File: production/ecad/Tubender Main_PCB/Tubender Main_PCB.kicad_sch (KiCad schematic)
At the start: 0 parts

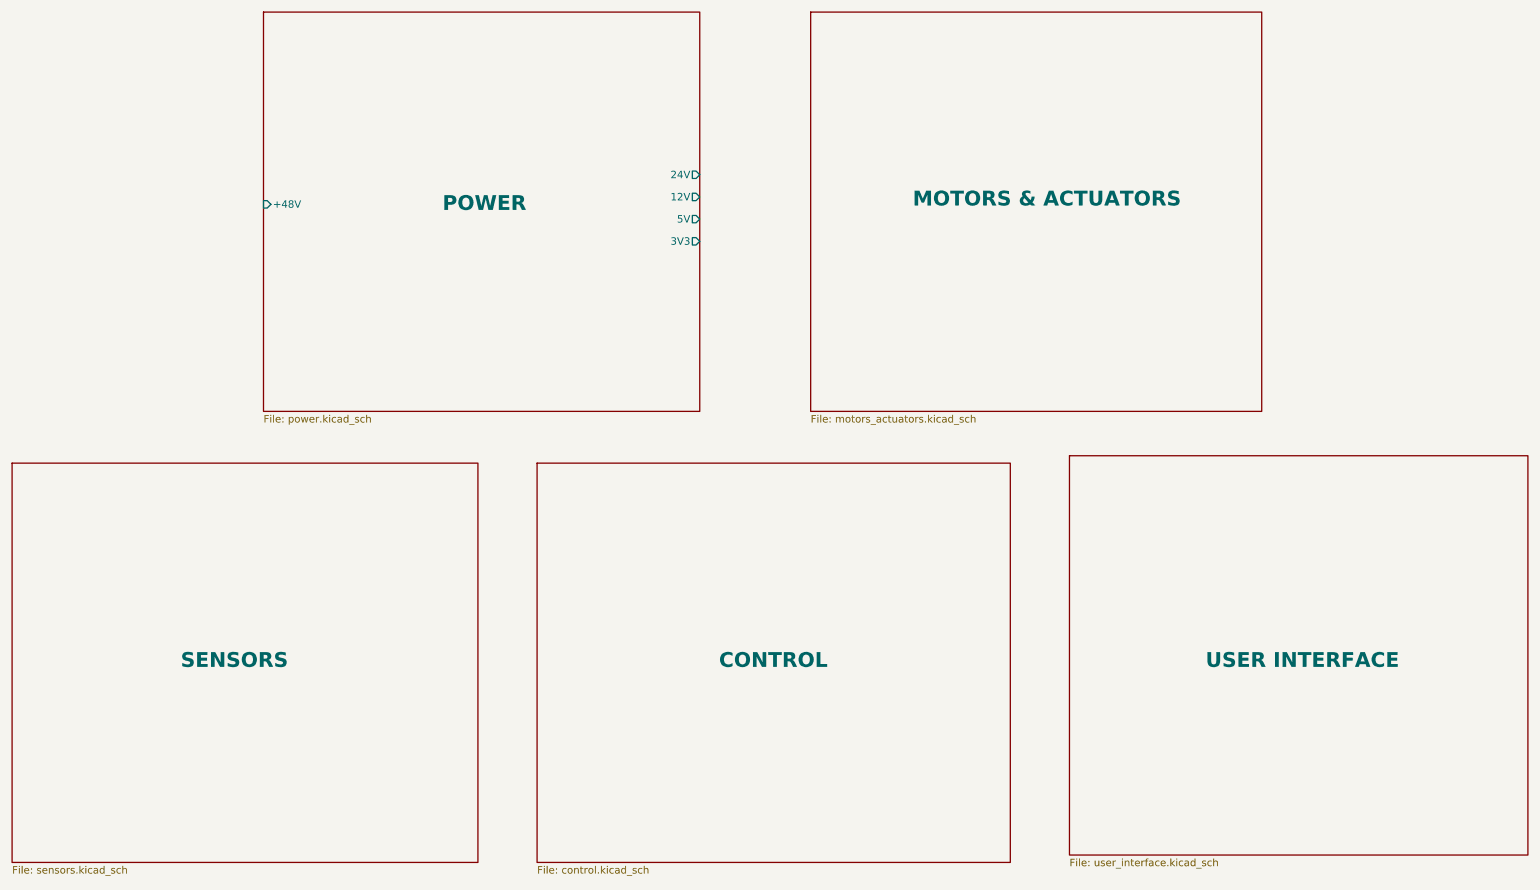
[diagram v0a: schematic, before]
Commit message: Separated into Two PCBS
UI and Main now seperated
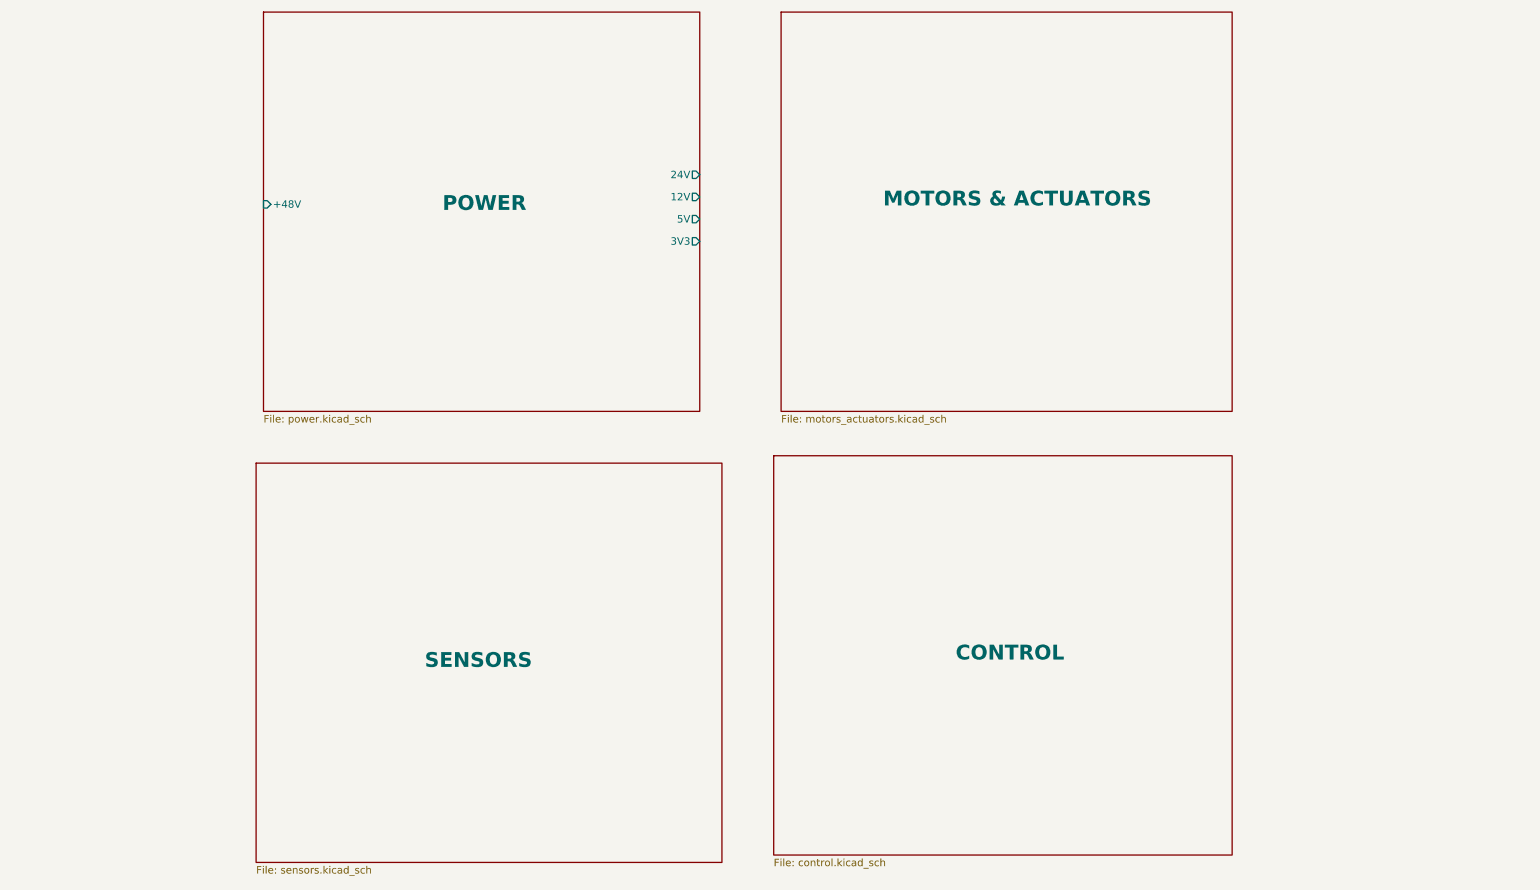
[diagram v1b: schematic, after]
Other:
- removed sheet USER INTERFACE
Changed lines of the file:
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@@
 	)
 	(sheet
-		(at 153.67 17.78)
+		(at 148.59 17.78)
 		(size 77.47 68.58)
 		(stroke
@@
 		)
 		(property "Sheetname" "MOTORS & ACTUATORS"
-			(at 171.196 51.308 0)
+			(at 166.116 51.308 0)
 			(effects
 				(font
@@
 		)
 		(property "Sheetfile" "motors_actuators.kicad_sch"
-			(at 153.67 86.9446 0)
+			(at 148.59 86.9446 0)
 			(effects
 				(font
@@
 		)
 		(instances
-			(project "Tubender PCB"
+			(project "Tubender Main_PCB"
 				(path "/3e1aedd0-6089-4edb-92c7-0c31da2e7927"
 					(page "3")
@@
 		)
 		(instances
-			(project "Tubender PCB"
+			(project "Tubender Main_PCB"
 				(path "/3e1aedd0-6089-4edb-92c7-0c31da2e7927"
 					(page "2")
@@
 	)
 	(sheet
-		(at 106.68 95.25)
-		(size 81.28 68.58)
+		(at 147.32 93.98)
+		(size 78.74 68.58)
 		(stroke
 			(width 0.1524)
@@
 		)
 		(property "Sheetname" "CONTROL"
-			(at 137.922 130.556 0)
+			(at 178.562 129.286 0)
 			(effects
 				(font
@@
 		)
 		(property "Sheetfile" "control.kicad_sch"
-			(at 106.68 164.4146 0)
+			(at 147.32 163.1446 0)
 			(effects
 				(font
@@
 		)
 		(instances
-			(project "Tubender PCB"
+			(project "Tubender Main_PCB"
 				(path "/3e1aedd0-6089-4edb-92c7-0c31da2e7927"
 					(page "5")
@@
 	)
 	(sheet
-		(at 16.51 95.25)
+		(at 58.42 95.25)
 		(size 80.01 68.58)
 		(stroke
@@
 		)
 		(property "Sheetname" "SENSORS"
-			(at 45.466 130.556 0)
+			(at 87.376 130.556 0)
 			(effects
 				(font
@@
 		)
 		(property "Sheetfile" "sensors.kicad_sch"
-			(at 16.51 164.4146 0)
+			(at 58.42 164.4146 0)
 			(effects
 				(font
@@
 		)
 		(instances
-			(project "Tubender PCB"
+			(project "Tubender Main_PCB"
 				(path "/3e1aedd0-6089-4edb-92c7-0c31da2e7927"
 					(page "4")
 				)
 			)
-		)
-	)
-	(sheet
-		(at 198.12 93.98)
-		(size 78.74 68.58)
-		(stroke
-			(width 0.1524)
-			(type solid)
-		)
-		(fill
-			(color 0 0 0 0.0000)
-		)
-		(property "Sheetname" "USER INTERFACE"
-			(at 221.488 130.556 0)
-			(effects
-				(font
-					(size 2.54 2.54)
-					(thickness 0.508)
-					(bold yes)
-				)
-				(justify left bottom)
-			)
-		)
-		(property "Sheetfile" "user_interface.kicad_sch"
-			(at 198.12 163.1446 0)
-			(effects
-				(font
-					(size 1.27 1.27)
-				)
-				(justify left top)
-			)
-		)
-		(instances
-			(project "Tubender PCB"
-				(path "/3e1aedd0-6089-4edb-92c7-0c31da2e7927"
-					(page "6")
-				)
-			)

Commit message: Fixed the Nets
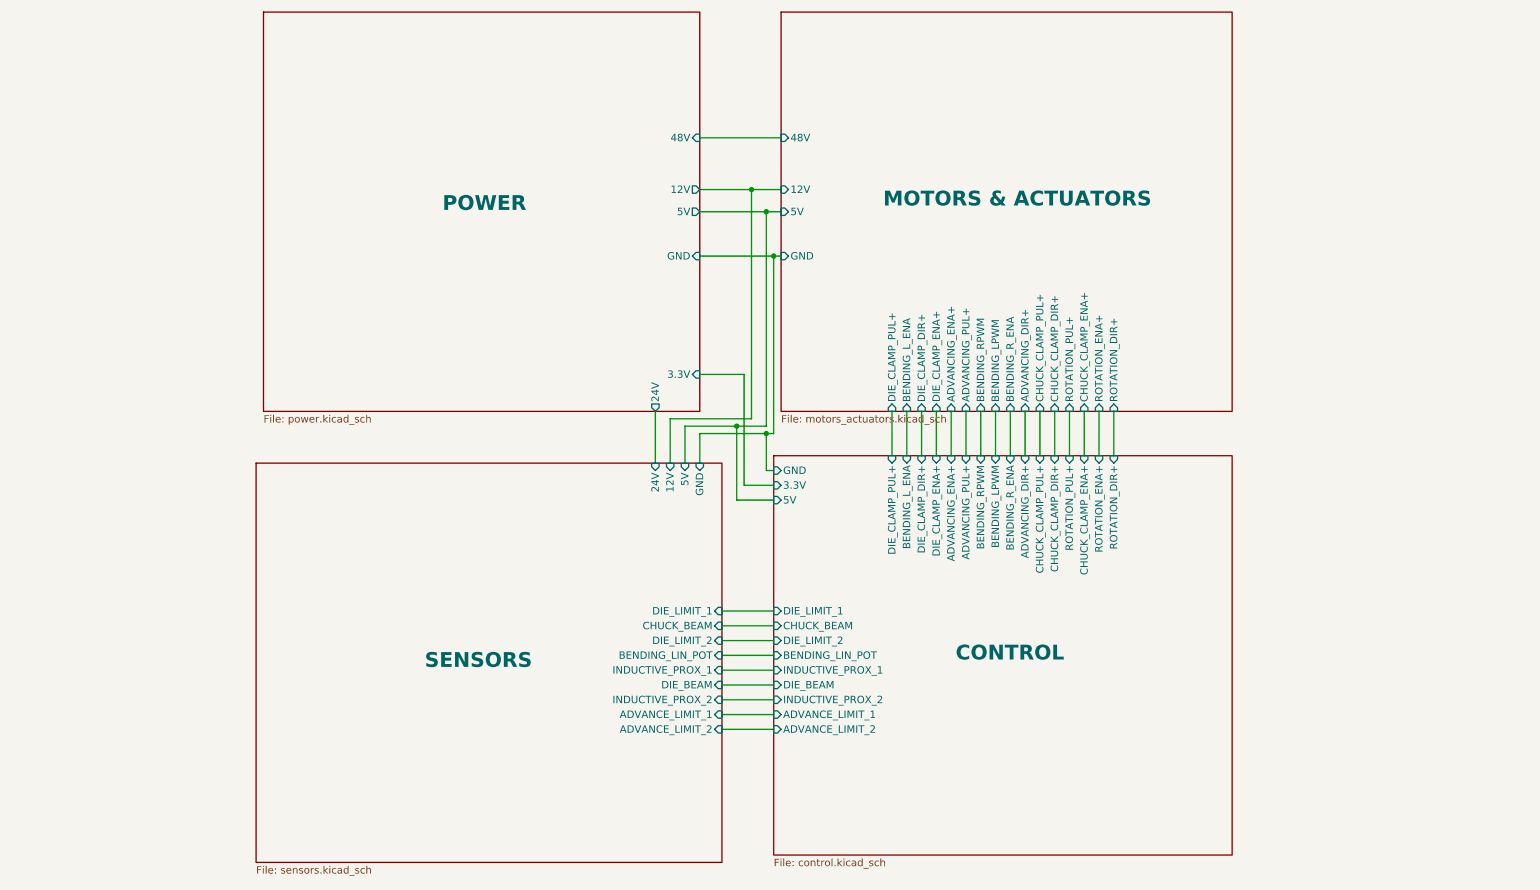
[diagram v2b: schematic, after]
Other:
- sheet CONTROL ports: added 3.3V, 5V, ADVANCE_LIMIT_1, ADVANCE_LIMIT_2, ADVANCING_DIR+, ADVANCING_ENA+, ADVANCING_PUL+, BENDING_LIN_POT, BENDING_LPWM, BENDING_L_ENA, BENDING_RPWM, BENDING_R_ENA, CHUCK_BEAM, CHUCK_CLAMP_DIR+, CHUCK_CLAMP_ENA+, CHUCK_CLAMP_PUL+, DIE_BEAM, DIE_CLAMP_DIR+, DIE_CLAMP_ENA+, DIE_CLAMP_PUL+, DIE_LIMIT_1, DIE_LIMIT_2, GND, INDUCTIVE_PROX_1, INDUCTIVE_PROX_2, ROTATION_DIR+, ROTATION_ENA+, ROTATION_PUL+; removed none
- sheet MOTORS & ACTUATORS ports: added 12V, 48V, 5V, ADVANCING_DIR+, ADVANCING_ENA+, ADVANCING_PUL+, BENDING_LPWM, BENDING_L_ENA, BENDING_RPWM, BENDING_R_ENA, CHUCK_CLAMP_DIR+, CHUCK_CLAMP_ENA+, CHUCK_CLAMP_PUL+, DIE_CLAMP_DIR+, DIE_CLAMP_ENA+, DIE_CLAMP_PUL+, GND, ROTATION_DIR+, ROTATION_ENA+, ROTATION_PUL+; removed none
- sheet POWER ports: added 3.3V, 48V, GND; removed +48V, 3V3
- sheet SENSORS ports: added 12V, 24V, 5V, ADVANCE_LIMIT_1, ADVANCE_LIMIT_2, BENDING_LIN_POT, CHUCK_BEAM, DIE_BEAM, DIE_LIMIT_1, DIE_LIMIT_2, GND, INDUCTIVE_PROX_1, INDUCTIVE_PROX_2; removed none
